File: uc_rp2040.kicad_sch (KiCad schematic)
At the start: 31 parts

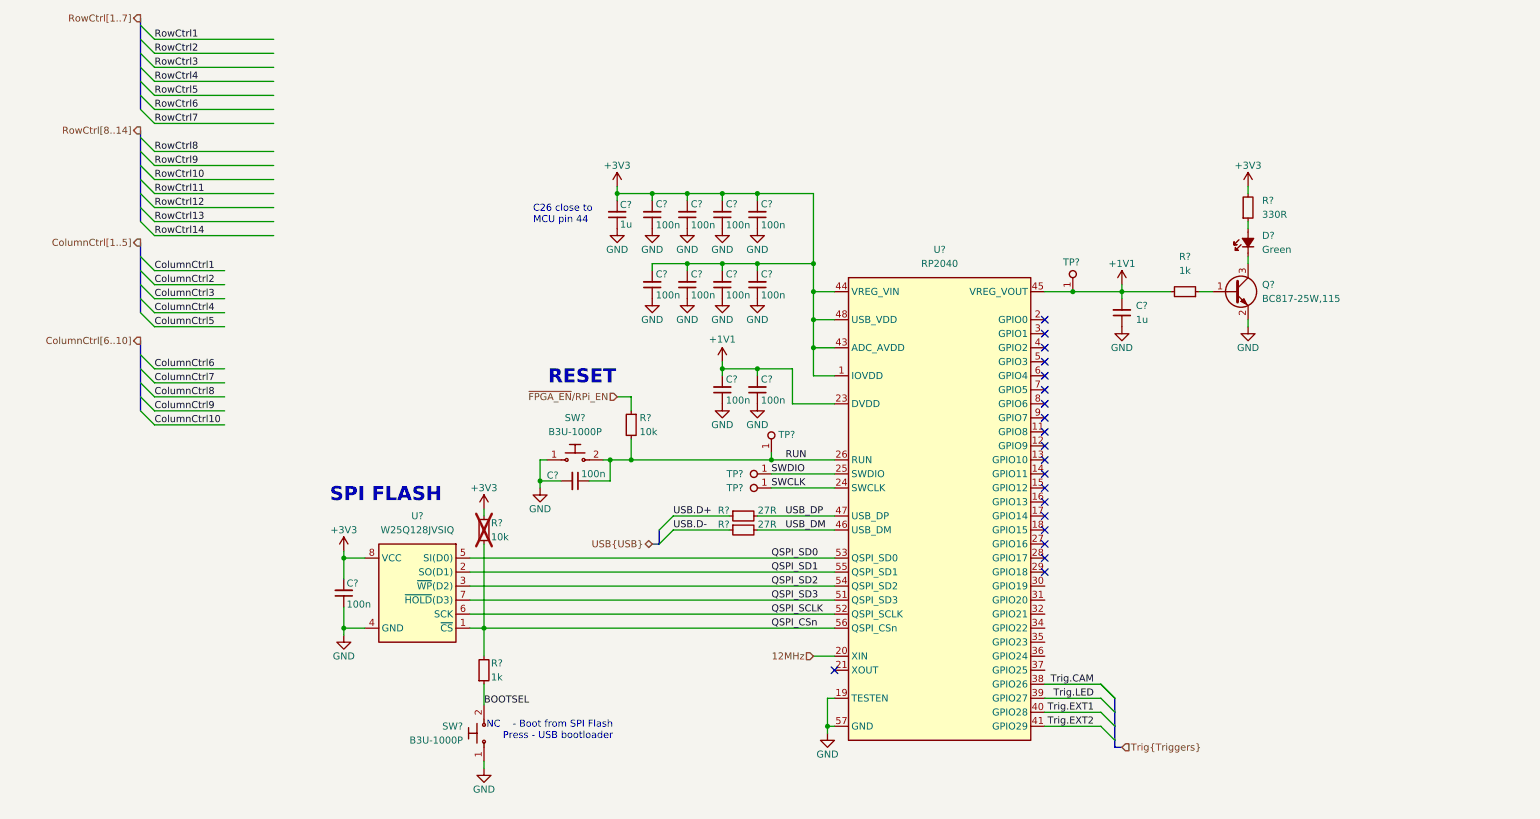
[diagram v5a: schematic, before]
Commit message: [#72133] Coonect matrix control signals to uC/FPGA
Signed-off-by: Dawid Lentka <dlentka@antmicro.com>
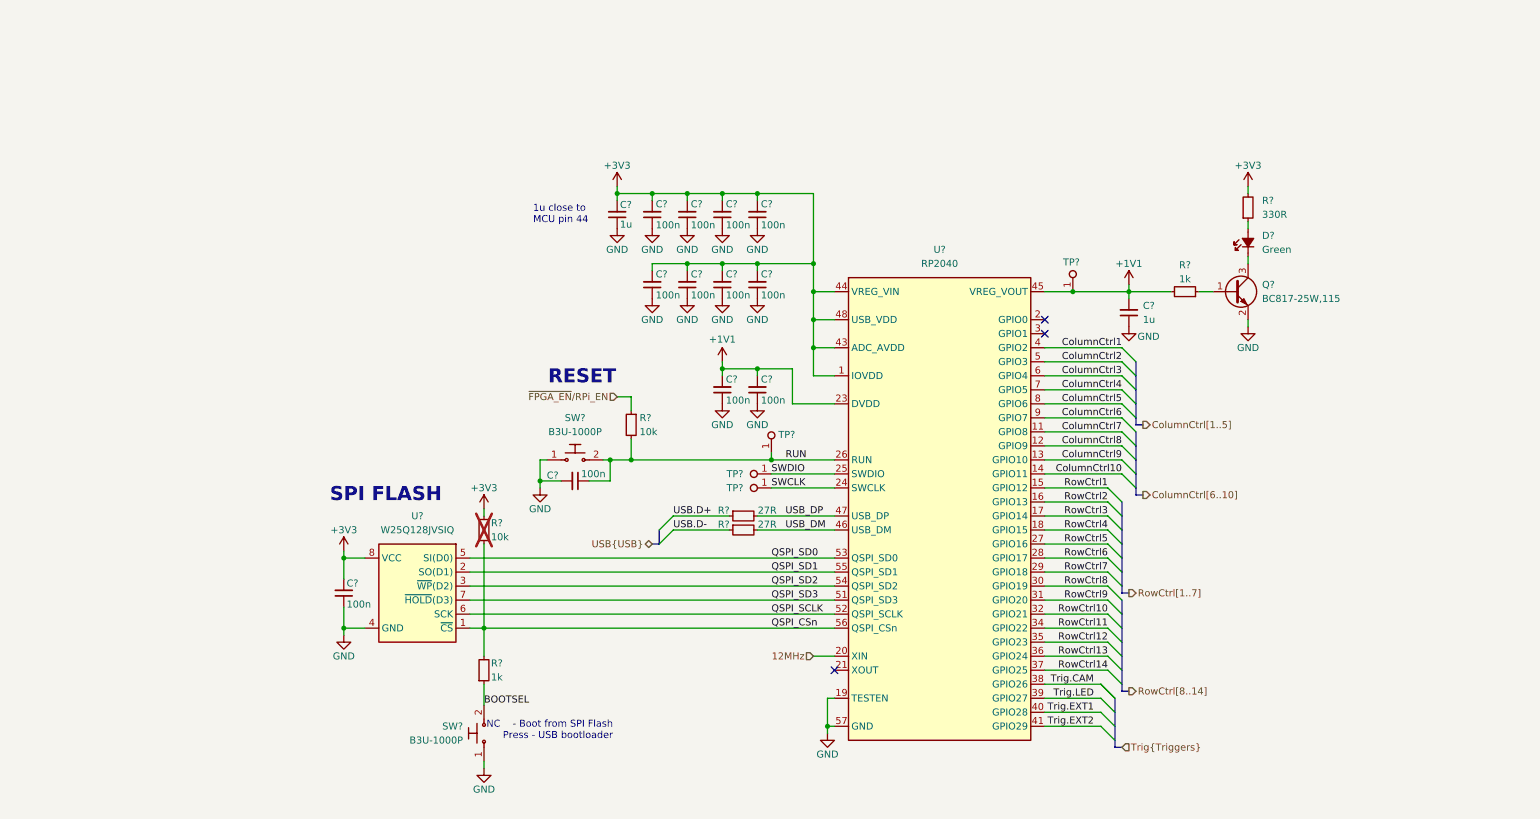
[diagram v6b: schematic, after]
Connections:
- net ColumnCtrl1: now also U?.4 (GPIO2)
- net ColumnCtrl10: now also U?.14 (GPIO11)
- net ColumnCtrl2: now also U?.5 (GPIO3)
- net ColumnCtrl3: now also U?.6 (GPIO4)
- net ColumnCtrl4: now also U?.7 (GPIO5)
- net ColumnCtrl5: now also U?.8 (GPIO6)
- net ColumnCtrl6: now also U?.9 (GPIO7)
- net ColumnCtrl7: now also U?.11 (GPIO8)
- net ColumnCtrl8: now also U?.12 (GPIO9)
- net ColumnCtrl9: now also U?.13 (GPIO10)
- net RowCtrl1: now also U?.15 (GPIO12)
- net RowCtrl10: now also U?.32 (GPIO21)
- net RowCtrl11: now also U?.34 (GPIO22)
- net RowCtrl12: now also U?.35 (GPIO23)
- net RowCtrl13: now also U?.36 (GPIO24)
- net RowCtrl14: now also U?.37 (GPIO25)
- net RowCtrl2: now also U?.16 (GPIO13)
- net RowCtrl3: now also U?.17 (GPIO14)
- net RowCtrl4: now also U?.18 (GPIO15)
- net RowCtrl5: now also U?.27 (GPIO16)
- net RowCtrl6: now also U?.28 (GPIO17)
- net RowCtrl7: now also U?.29 (GPIO18)
- net RowCtrl8: now also U?.30 (GPIO19)
- net RowCtrl9: now also U?.31 (GPIO20)
- no-connect marks 20 -> 3
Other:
- note added: "1u close to MCU pin 44"
- note removed: "C26 close to MCU pin 44"
- moved on the sheet: C?

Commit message: [#72133] Annotate schematics
Signed-off-by: Dawid Lentka <dlentka@antmicro.com>
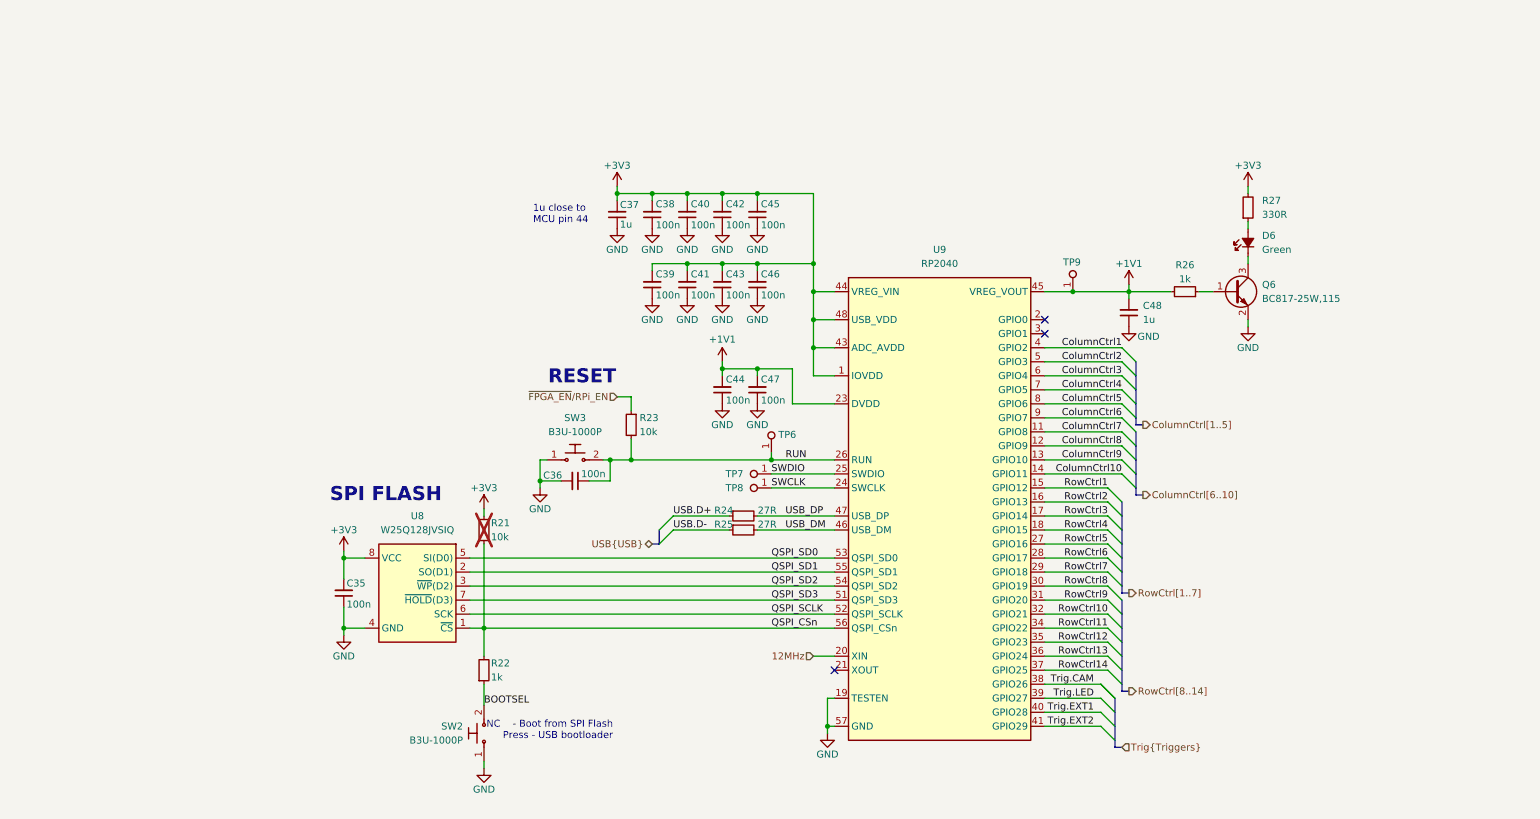
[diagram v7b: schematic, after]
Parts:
- gave numbers to parts that had none: 31

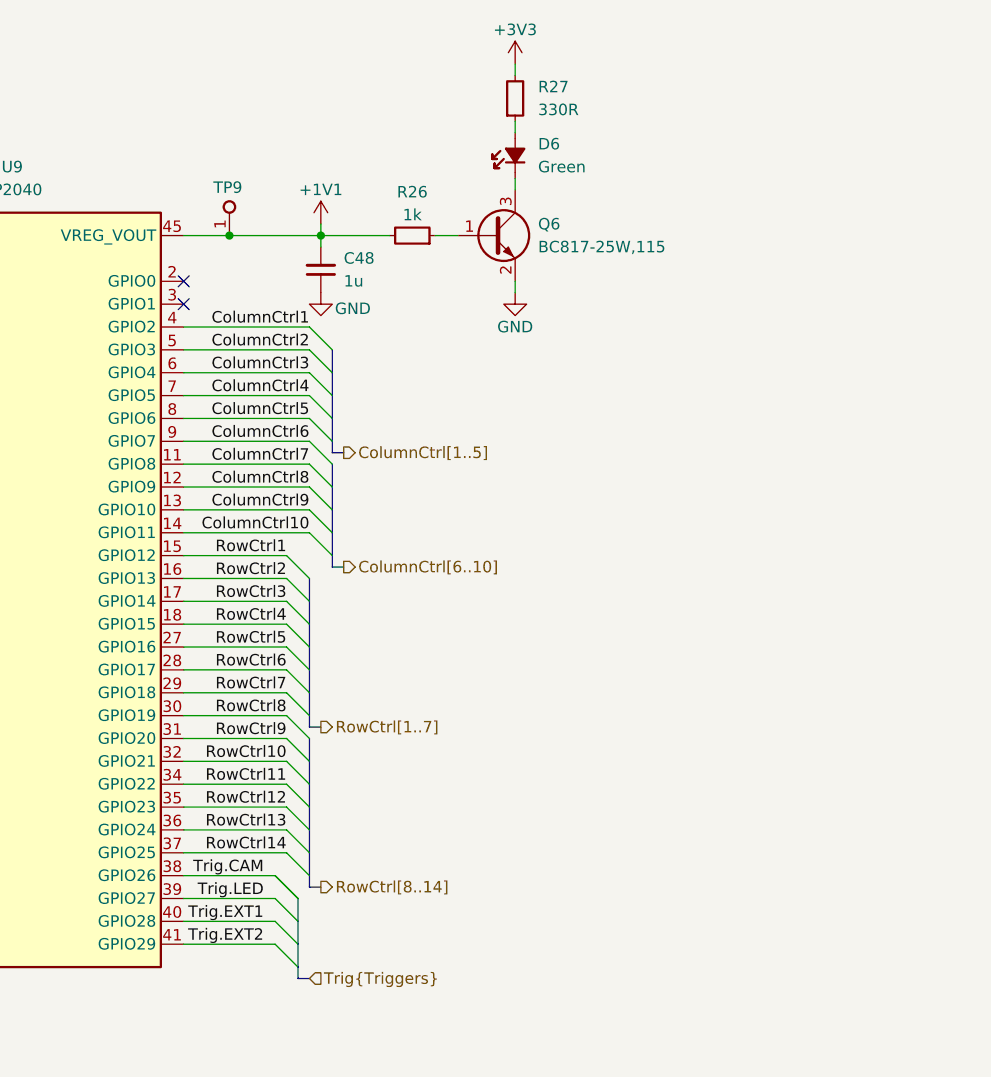
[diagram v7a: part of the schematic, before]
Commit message: [#72133] Sch: Add IMU
Signed-off-by: Dawid Lentka <dlentka@antmicro.com>
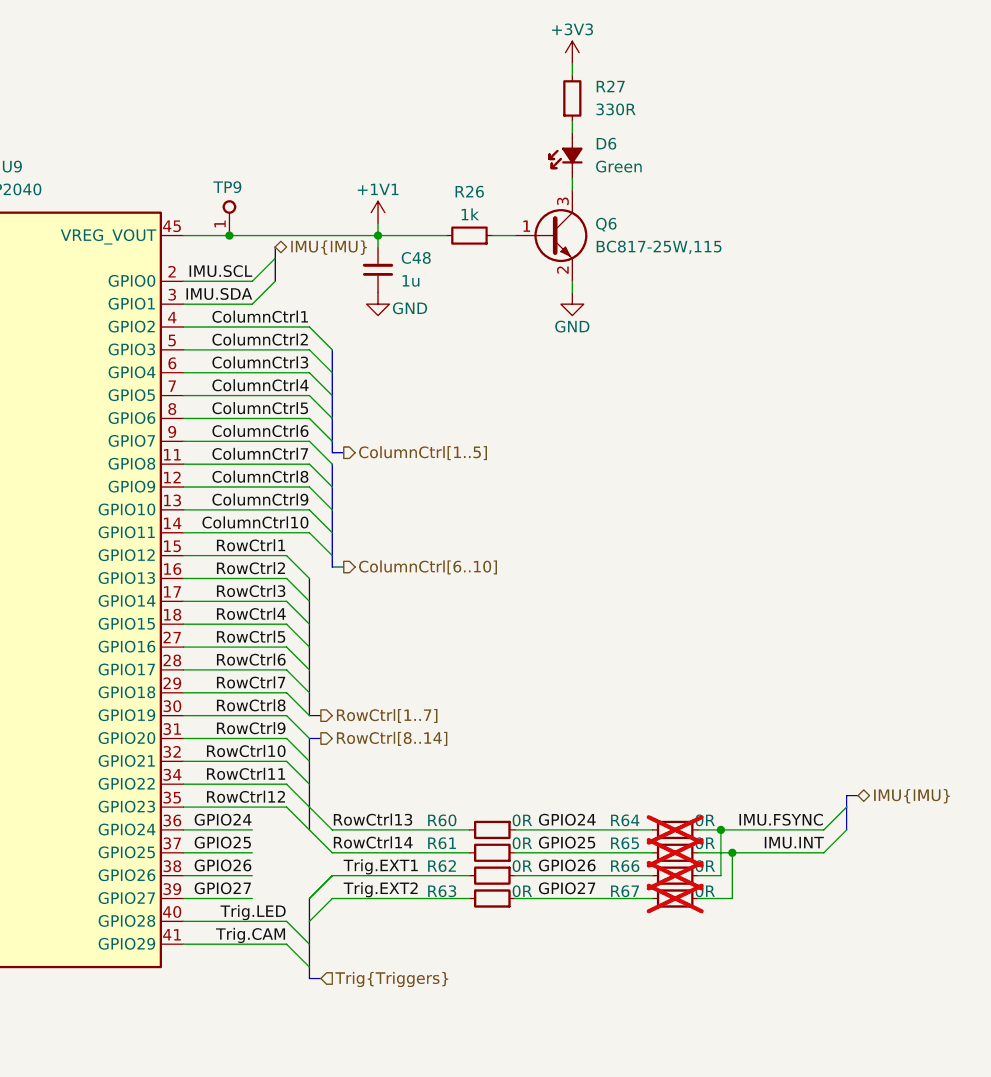
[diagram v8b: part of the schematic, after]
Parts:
- added R60, R61, R62, R63, R64, R65, R66, R67: R_0R_0402, antmicro-footprints:R_0402_1005Metric, symbol antmicroResistors0402:R_0R_0402
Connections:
- net RowCtrl13: now also R60.2; no longer U9.36 (GPIO24)
- net RowCtrl14: now also R61.2; no longer U9.37 (GPIO25)
- net Trig.CAM: now also U9.41 (GPIO29); no longer U9.38 (GPIO26)
- net Trig.EXT1: now also R62.2; no longer U9.40 (GPIO28)
- net Trig.EXT2: now also R63.2; no longer U9.41 (GPIO29)
- net Trig.LED: now also U9.40 (GPIO28); no longer U9.39 (GPIO27)
- net IMU.SCL: now reaches U9.2 (GPIO0)
- net IMU.SDA: now reaches U9.3 (GPIO1)
- new net GPIO24: R60.1, R64.2, U9.36 (GPIO24)
- new net GPIO25: R61.1, R65.2, U9.37 (GPIO25)
- new net GPIO26: R62.1, R66.2, U9.38 (GPIO26)
- new net GPIO27: R63.1, R67.2, U9.39 (GPIO27)
- new net IMU.FSYNC: R64.1, R66.1
- new net IMU.INT: R65.1, R67.1
- no-connect marks 3 -> 1
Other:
- moved on the sheet: C48, D6, Q6, R26, R27
